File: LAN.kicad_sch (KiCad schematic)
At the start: 1 part, among them U4 WIZ850io

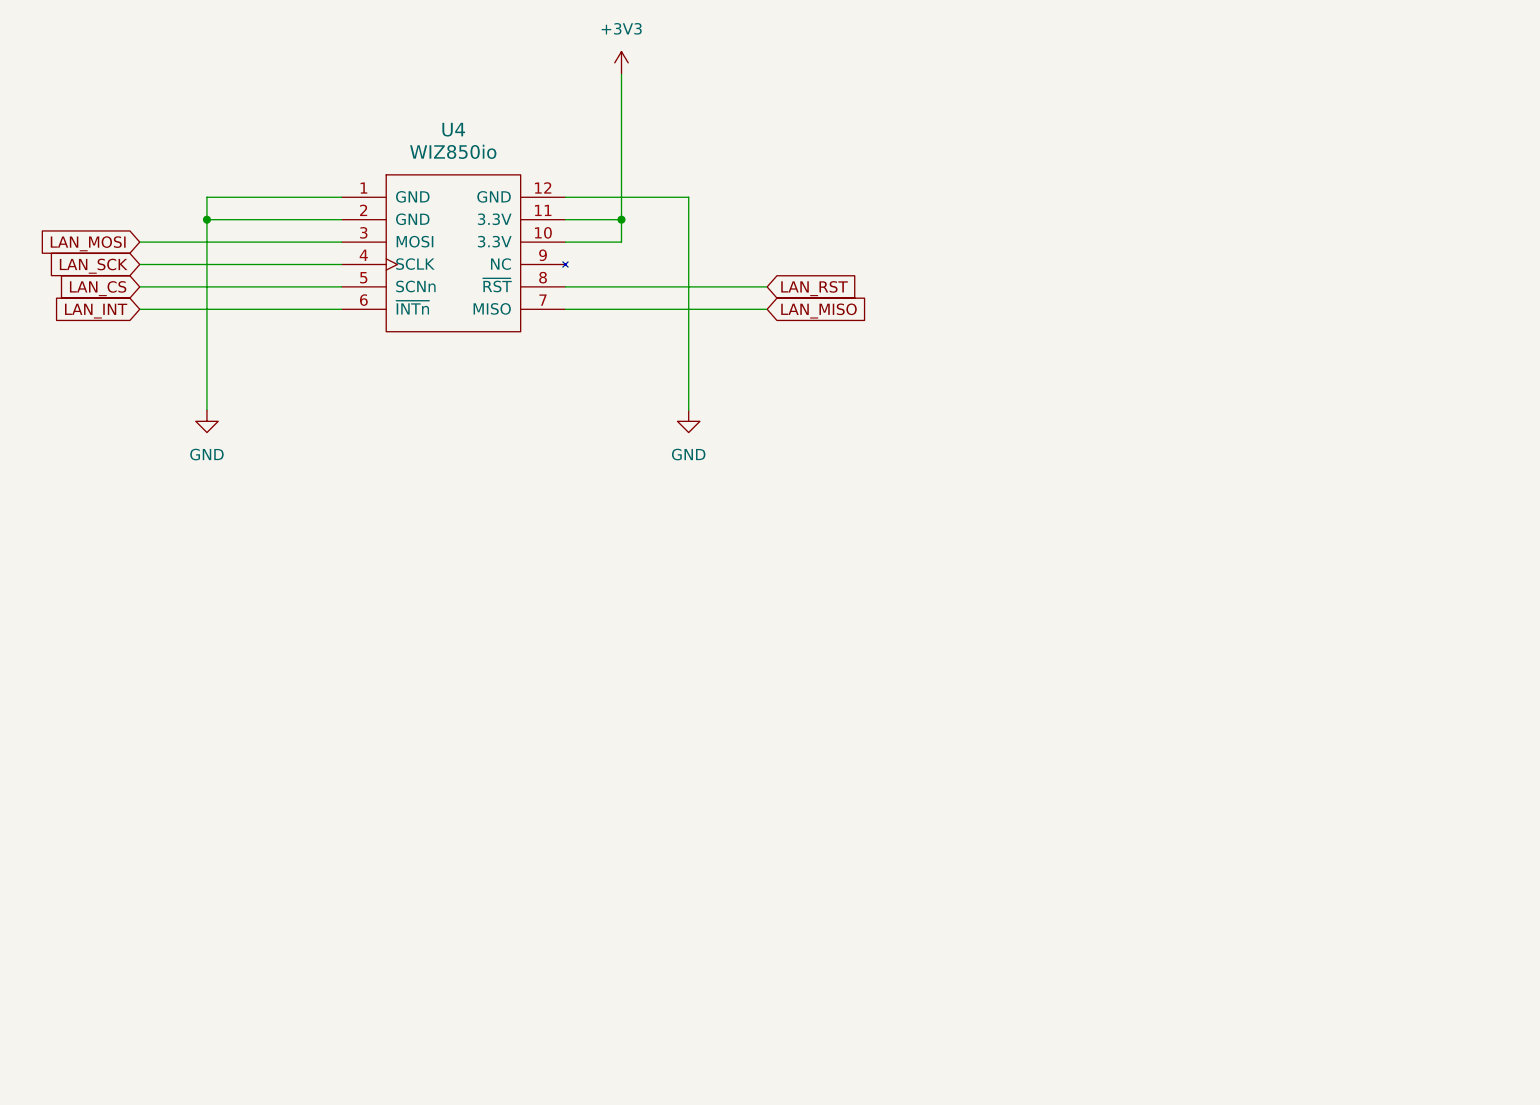
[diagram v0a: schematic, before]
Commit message: Connect W5500 to ESP32, fix RFID SCK, add relay flyback diode
- ESP32: add global labels LAN_CS/RST/INT/SCK/MISO/MOSI on GPIO 5/6/7/14/15/16
  (matches WIRING_OVERVIEW.md)
- ESP32: rename SCK label to RFID_SCK so GPIO12 reaches PN532 connector J1
- ESP32: connect WAKE_UP (optocoupler U3) to GPIO21
- LAN: power WIZ850io from +3.3V instead of unconnected +3V3 net
- Interfaces: add flyback diode D5 (1N4148W, LCSC C81598) across K1 coil
- Interfaces: tie R12 pull-up to +3.3V, set value to 10k
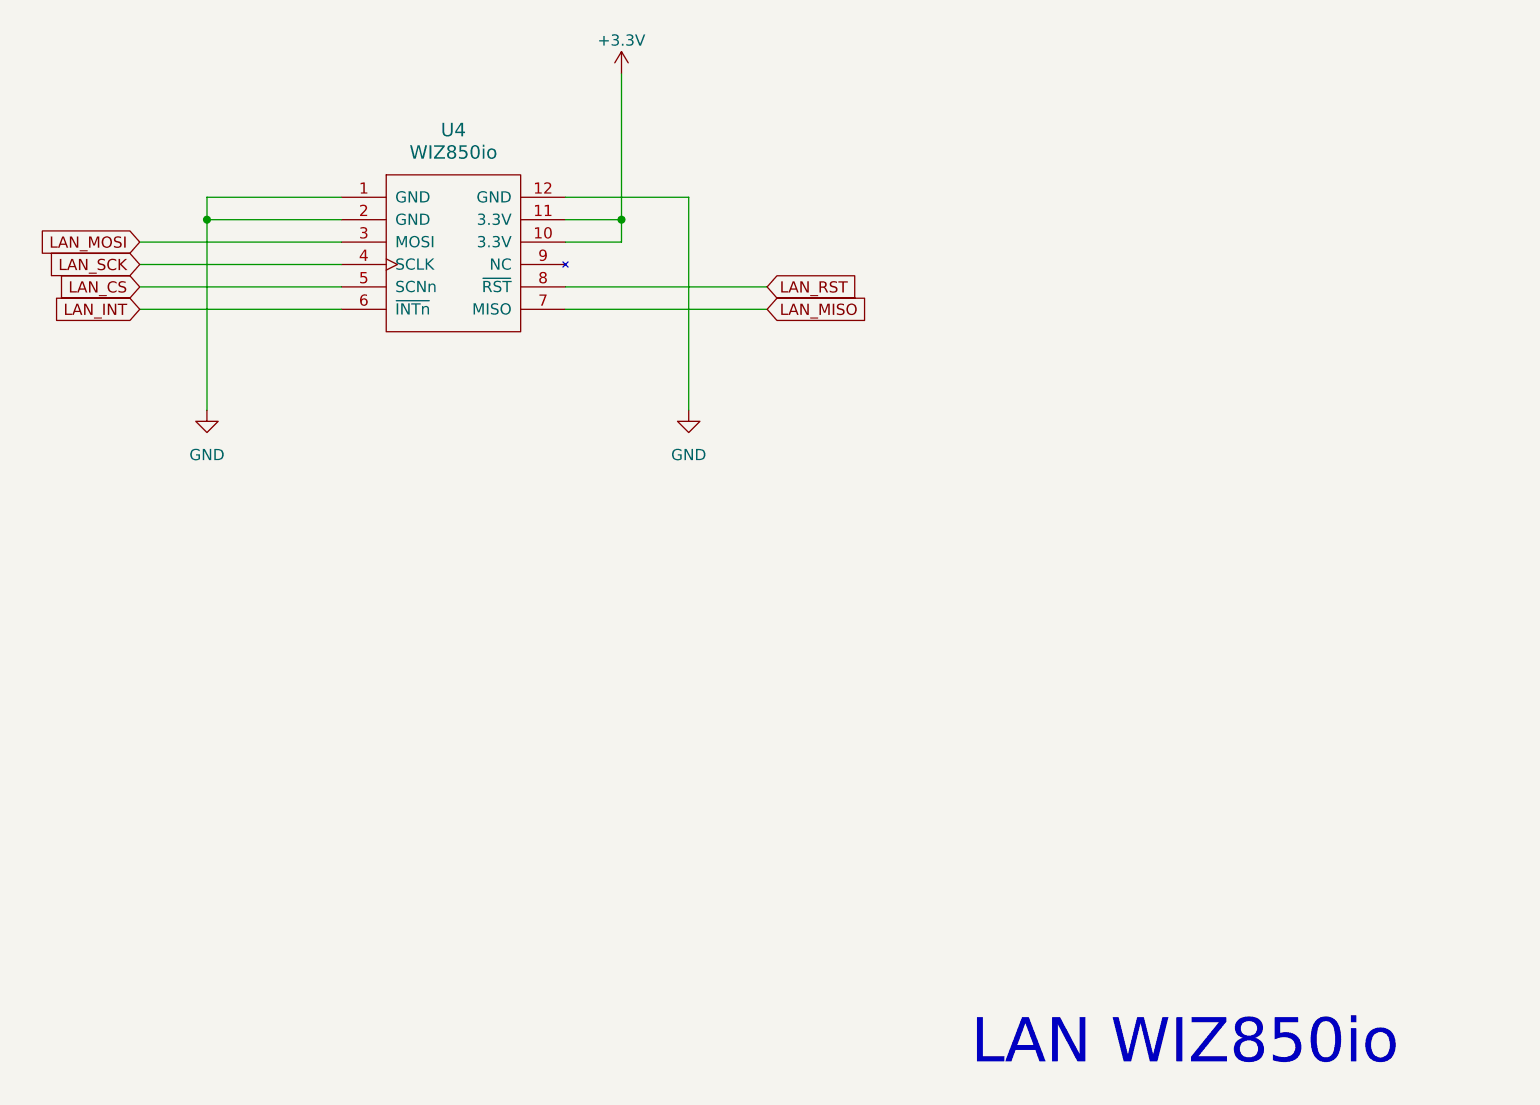
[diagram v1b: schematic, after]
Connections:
- net +3V3 renamed +3.3V
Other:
- note added: "LAN WIZ850io"
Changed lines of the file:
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@@
 	(generator_version "10.0")
 	(paper "A4")
+	(text "LAN WIZ850io"
+		(exclude_from_sim no)
+		(at 203.454 177.546 0)
+		(effects
+			(font
+				(size 5 5)
+			)
+			(justify left bottom)
+		)
+	)
 	(junction
 		(at 163.83 81.28)
@@
 	)
 	(symbol
+		(lib_id "power:+3.3V")
+		(at 163.83 64.77 0)
+		(unit 1)
+		(body_style 1)
+		(exclude_from_sim no)
+		(in_bom yes)
+		(on_board yes)
+		(in_pos_files yes)
+		(dnp no)
+		(fields_autoplaced yes)
+		(property "Reference" "#PWR041"
+			(at 163.83 68.58 0)
+			(hide yes)
+			(show_name no)
+			(do_not_autoplace no)
+			(effects
+				(font
+					(size 1.27 1.27)
+				)
+			)
+		)
+		(property "Value" "+3.3V"
+			(at 163.83 60.96 0)
+			(show_name no)
+			(do_not_autoplace no)
+			(effects
+				(font
+					(size 1.27 1.27)
+				)
+			)
+		)
+		(property "Footprint" ""
+			(at 163.83 64.77 0)
+			(hide yes)
+			(show_name no)
+			(do_not_autoplace no)
+			(effects
+				(font
+					(size 1.27 1.27)
+				)
+			)
+		)
+		(property "Datasheet" ""
+			(at 163.83 64.77 0)
+			(hide yes)
+			(show_name no)
+			(do_not_autoplace no)
+			(effects
+				(font
+					(size 1.27 1.27)
+				)
+			)
+		)
+		(property "Description" ""
+			(at 163.83 64.77 0)
+			(show_name no)
+			(do_not_autoplace no)
+			(effects
+				(font
+					(size 1.27 1.27)
+				)
+			)
+		)
+		(pin "1"
+		)
+		(instances
+			(project "GA_Fuelstation_Terminal"
+				(path "/9d5c9b65-fa9a-4f2b-b8e4-a4447f224f28/5c390488-d45b-4ef2-a073-15e25f367981"
+					(reference "#PWR041")
+					(unit 1)
+				)
+			)
+		)
+	)
+	(symbol
 		(lib_id "GA_Fuelstation_Terminal:WIZ850io")
 		(at 144.78 85.09 0)
@@
 					(unit 1)
 				)
-			)
-		)
-	)
-	(symbol
-		(lib_id "power:+3V3")
-		(at 163.83 64.77 0)
-		(unit 1)
-		(body_style 1)
-		(exclude_from_sim no)
-		(in_bom yes)
-		(on_board yes)
-		(in_pos_files yes)
-		(dnp no)
-		(fields_autoplaced yes)
-		(property "Reference" "#PWR041"
-			(at 163.83 68.58 0)
-			(hide yes)
-			(show_name no)
-			(do_not_autoplace no)
-			(effects
-				(font
-					(size 1.27 1.27)
-				)
-			)
-		)
-		(property "Value" "+3V3"
-			(at 163.83 59.69 0)
-			(show_name no)
-			(do_not_autoplace no)
-			(effects
-				(font
-					(size 1.27 1.27)
-				)
-			)
-		)
-		(property "Footprint" ""
-			(at 163.83 64.77 0)
-			(hide yes)
-			(show_name no)
-			(do_not_autoplace no)
-			(effects
-				(font
-					(size 1.27 1.27)
-				)
-			)
-		)
-		(property "Datasheet" ""
-			(at 163.83 64.77 0)
-			(hide yes)
-			(show_name no)
-			(do_not_autoplace no)
-			(effects
-				(font
-					(size 1.27 1.27)
-				)
-			)
-		)
-		(property "Description" "Power symbol creates a global label with name \"+3V3\""
-			(at 163.83 64.77 0)
-			(hide yes)
-			(show_name no)
-			(do_not_autoplace no)
-			(effects
-				(font
-					(size 1.27 1.27)
-				)
-			)
-		)
-		(pin "1"
-		)
-		(instances
-			(project "GA_Fuelstation_Terminal"
-				(path "/9d5c9b65-fa9a-4f2b-b8e4-a4447f224f28/5c390488-d45b-4ef2-a073-15e25f367981"
-					(reference "#PWR041")
-					(unit 1)
-				)
